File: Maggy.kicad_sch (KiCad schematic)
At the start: 75 parts, among them CN1 0430450800, CN2 430451000, U11 LM1117S-5.0, U12 LM1117S-3.3, U13 TLV2372IDR, U14 A4950ELJTR-T, U15 INA214AIDCKR, U16 INA214AIDCKR, U17 A4950ELJTR-T, U18 INA214AIDCKR, U19 INA214AIDCKR, U2 A4950ELJTR-T, U20 TMAG5170A2DGKR, U21 TMAG5170A2DGKR, U22 TMAG5170A2DGKR, U23 TMAG5170A2DGKR, U24 TMAG5170A2DGKR, U25 Socket for Teensy 4.1 (2x 1x2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, U3 CH224K, U4 BZT52C6V2, U5 XY308-2.54-2P, U6 XY308-2.54-2P, U7 XY308-2.54-2P, U8 XY308-2.54-2P, U9 A4950ELJTR-T

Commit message: chore: replace EasyEDA power regulator symbols with KiCad native ones
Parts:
- U11: footprint ProPrj_Maggy 4.1_2025-02-07-import-fps:SOT-223-3_L6.5-W3.4-P2.30-LS7.0-BR -> Package_TO_SOT_SMD:TO-263-3_TabPin2; symbol ProPrj_Mag-easyedapro:LM1117S-5.0 -> Regulator_Linear:LM1117S-5.0
- U12: footprint ProPrj_Maggy 4.1_2025-02-07-import-fps:SOT-223-3_L6.5-W3.4-P2.30-LS7.0-BR -> Package_TO_SOT_SMD:TO-263-3_TabPin2; symbol ProPrj_Mag-easyedapro:LM1117S-3.3 -> Regulator_Linear:LM1117S-3.3
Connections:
- net +3V3: no longer U12.4 (TAB)
- net +5V: now also U25.48 (VIN); no longer U11.4 (TAB), U25.49 (VUSB)
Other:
- moved on the sheet: C1, C10, C11, LED1, LED3, LED4, U3

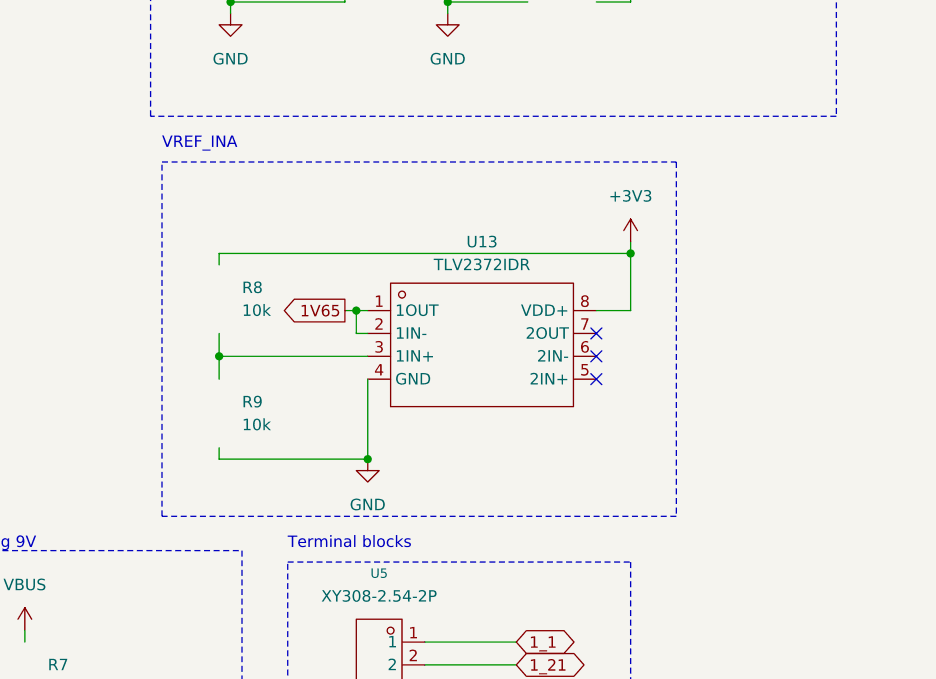
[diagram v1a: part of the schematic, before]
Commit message: chore: replace EasyEDA op-amp symbol with KiCad native three-part one
Replaced op-amp symbol for the part of the schematic generating the 1.65V reference for current sensing with a native KiCad symbol for the same op-amp. The new symbol is split into three parts instead of being a single block.
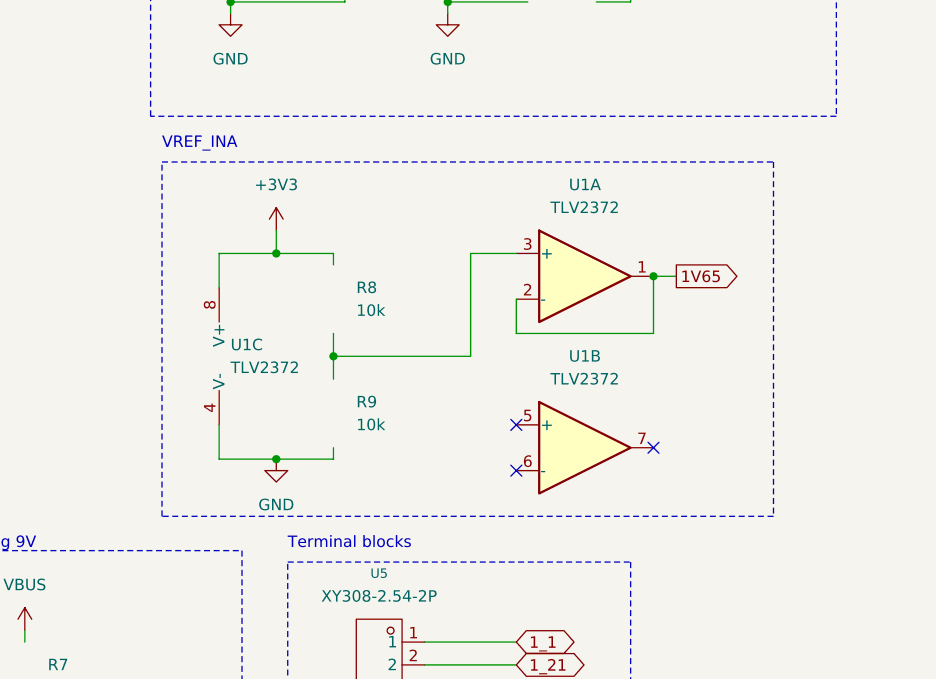
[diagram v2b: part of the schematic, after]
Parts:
- removed U13: TLV2372IDR, ProPrj_Maggy 4.1_2025-02-07-import-fps:SOIC-8_L4.9-W3.9-P1.27-LS6.0-BL, symbol ProPrj_Mag-easyedapro:TLV2372IDR
- added U1: TLV2372, symbol Amplifier_Operational:TLV2372
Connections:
- net +3V3: now also U1.8 (V+)
- net 1V65: now also U1.1, U1.2 (-)
- net GND: now also U1.4 (V-)
- net at R8.1, R9.2: now also U1.3 (+)

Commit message: chore: add footprint to new op-amp symbols
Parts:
- U1: footprint (none) -> Package_SO:SOIC-8_3.9x4.9mm_P1.27mm
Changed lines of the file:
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@@
 			)
 		)
-		(property "Footprint" ""
+		(property "Footprint" "Package_SO:SOIC-8_3.9x4.9mm_P1.27mm"
 			(at 165.1 132.08 0)
 			(hide yes)
@@
 			)
 		)
-		(property "Footprint" ""
+		(property "Footprint" "Package_SO:SOIC-8_3.9x4.9mm_P1.27mm"
 			(at 165.1 113.03 0)
 			(hide yes)
@@
 			)
 		)
-		(property "Footprint" ""
+		(property "Footprint" "Package_SO:SOIC-8_3.9x4.9mm_P1.27mm"
 			(at 127 121.92 0)
 			(hide yes)

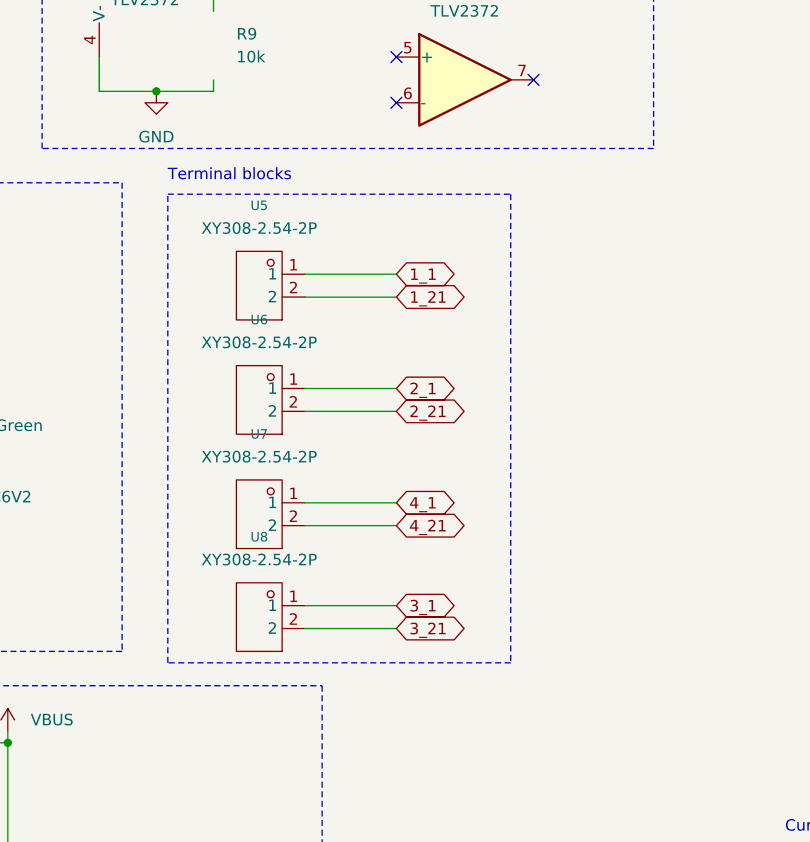
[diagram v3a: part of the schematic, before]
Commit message: chore: replace EasyEDA screw terminals with KiCad native ones
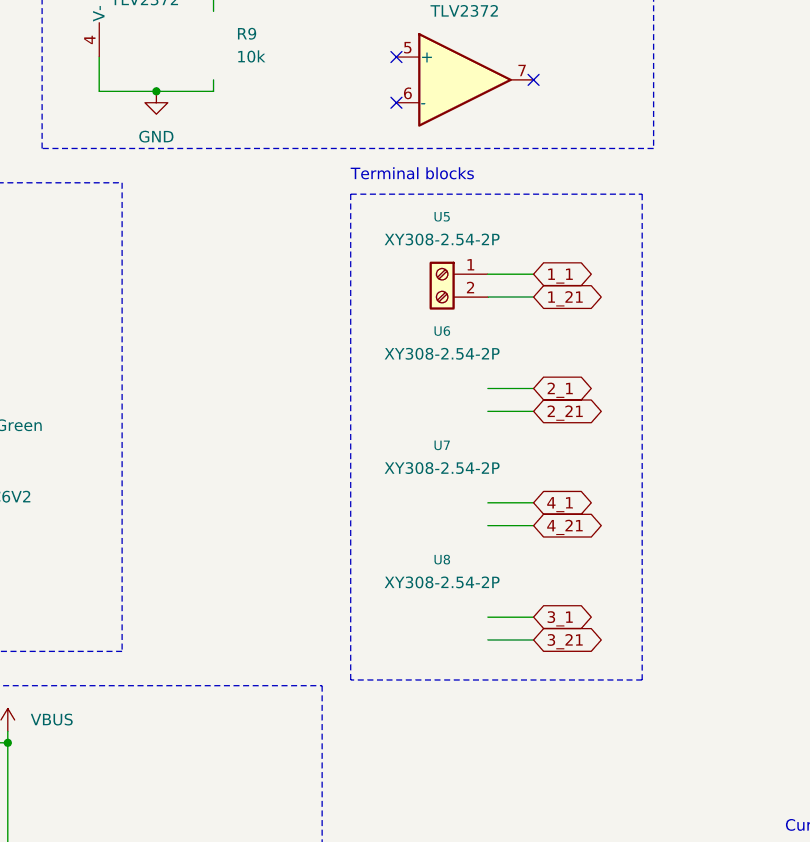
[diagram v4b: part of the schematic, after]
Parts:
- U5, U6, U7, U8: symbol ProPrj_Mag-easyedapro:XY308-2.54-2P -> Connector:Screw_Terminal_01x02

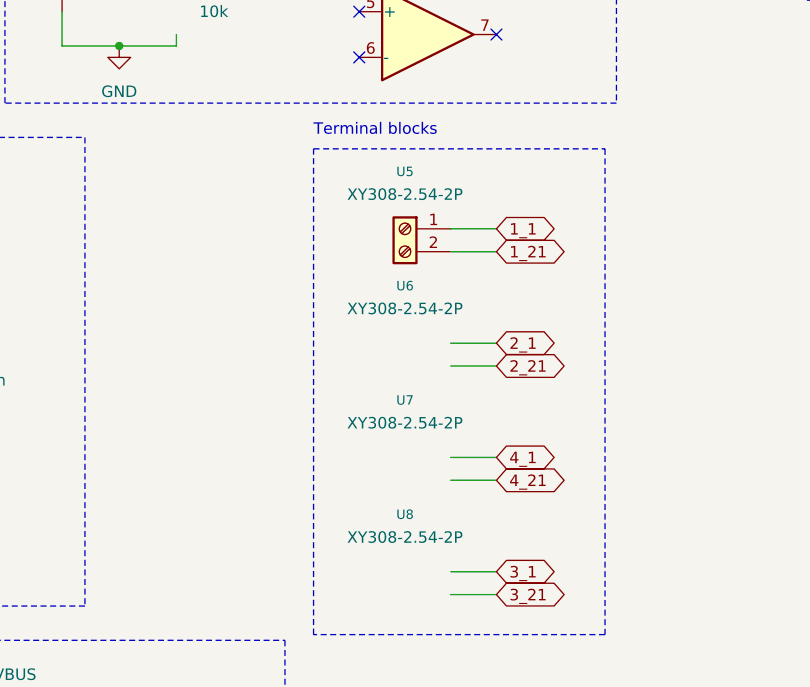
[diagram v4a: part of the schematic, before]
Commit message: chore: update references for screw terminals to match common convention
The naming for references for the screw terminals were prefixed with U-, which is usually reserved for integrated circuits. They have been replaced with J- references.
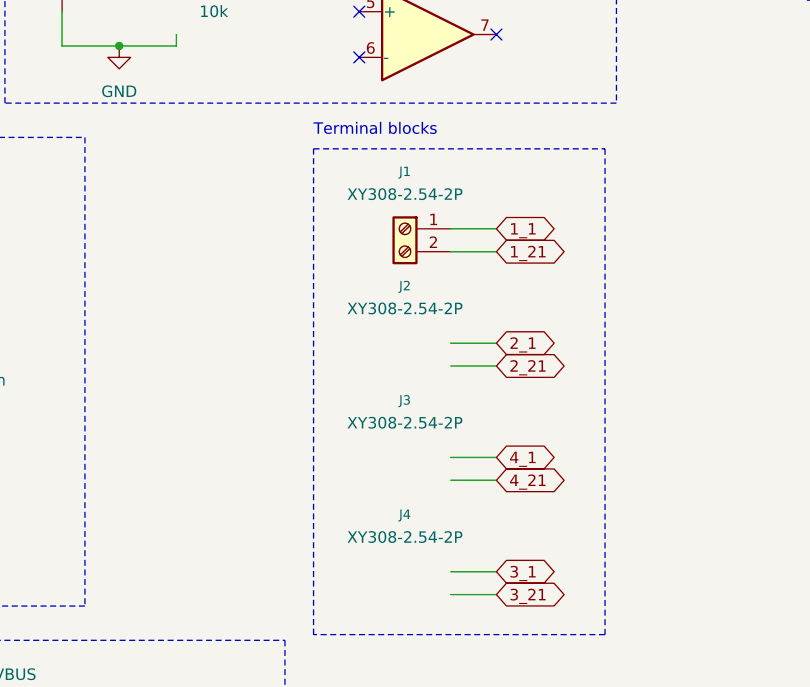
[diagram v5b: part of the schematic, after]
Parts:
- renumbered U5 to J1, U6 to J2, U7 to J3, U8 to J4
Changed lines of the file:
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@@
 		(dnp no)
 		(fields_autoplaced yes)
-		(property "Reference" "U6"
+		(property "Reference" "J2"
 			(at 162.56 160.02 0)
 			(show_name no)
@@
 			(project "Maggy"
 				(path "/52283d6a-1d9f-44e8-81a2-e61315819c23"
-					(reference "U6")
+					(reference "J2")
 					(unit 1)
 				)
@@
 		(dnp no)
 		(fields_autoplaced yes)
-		(property "Reference" "U8"
+		(property "Reference" "J4"
 			(at 162.56 185.42 0)
 			(show_name no)
@@
 			(project "Maggy"
 				(path "/52283d6a-1d9f-44e8-81a2-e61315819c23"
-					(reference "U8")
+					(reference "J4")
 					(unit 1)
 				)
@@
 		(dnp no)
 		(fields_autoplaced yes)
-		(property "Reference" "U7"
+		(property "Reference" "J3"
 			(at 162.56 172.72 0)
 			(show_name no)
@@
 			(project "Maggy"
 				(path "/52283d6a-1d9f-44e8-81a2-e61315819c23"
-					(reference "U7")
+					(reference "J3")
 					(unit 1)
 				)
@@
 		(dnp no)
 		(fields_autoplaced yes)
-		(property "Reference" "U5"
+		(property "Reference" "J1"
 			(at 162.56 147.32 0)
 			(show_name no)
@@
 			(project "Maggy"
 				(path "/52283d6a-1d9f-44e8-81a2-e61315819c23"
-					(reference "U5")
+					(reference "J1")
 					(unit 1)
 				)
